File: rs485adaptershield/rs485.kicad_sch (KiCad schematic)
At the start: 13 parts, among them U10 MAX485E

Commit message: more work
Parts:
- removed C1: 100n, Capacitor_SMD:C_0805_2012Metric, symbol Device:C
- removed R2, R3, R4: 10k, Resistor_SMD:R_0805_2012Metric, symbol Device:R
- removed U10: MAX485E, Package_SO:SOIC-8_3.9x4.9mm_P1.27mm, symbol Interface_UART:MAX485E
- added C21: 100n, Capacitor_SMD:C_0603_1608Metric, symbol Device:C
- added IC2: THVD1406DRLR, SOTFL50P160X60-8N, symbol THVD1406DRLR:THVD1406DRLR
- added R13: 10k, Resistor_SMD:R_0805_2012Metric, symbol Device:R
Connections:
- net DI is gone; now on net ¬RE: R5.2
- net +5V: now also C21.2, IC2.8 (VCC), R13.1
- net GND: now also C21.1, IC2.5 (GND)
- net ¬RE: now also IC2.2 (~{RE})
- net A+ renamed A
- net B- renamed B
- new net: IC2.3 (~{SHDN}), R13.2
- new net D: IC2.4 (D)
- new net R: IC2.1 (R)
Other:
- moved on the sheet: D2, D3, F2, F3, R6, R7, R8

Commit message: more progress
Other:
- moved on the sheet: C21, D2, D3, F2, F3, IC2, R13, R5, R6, R7, R8

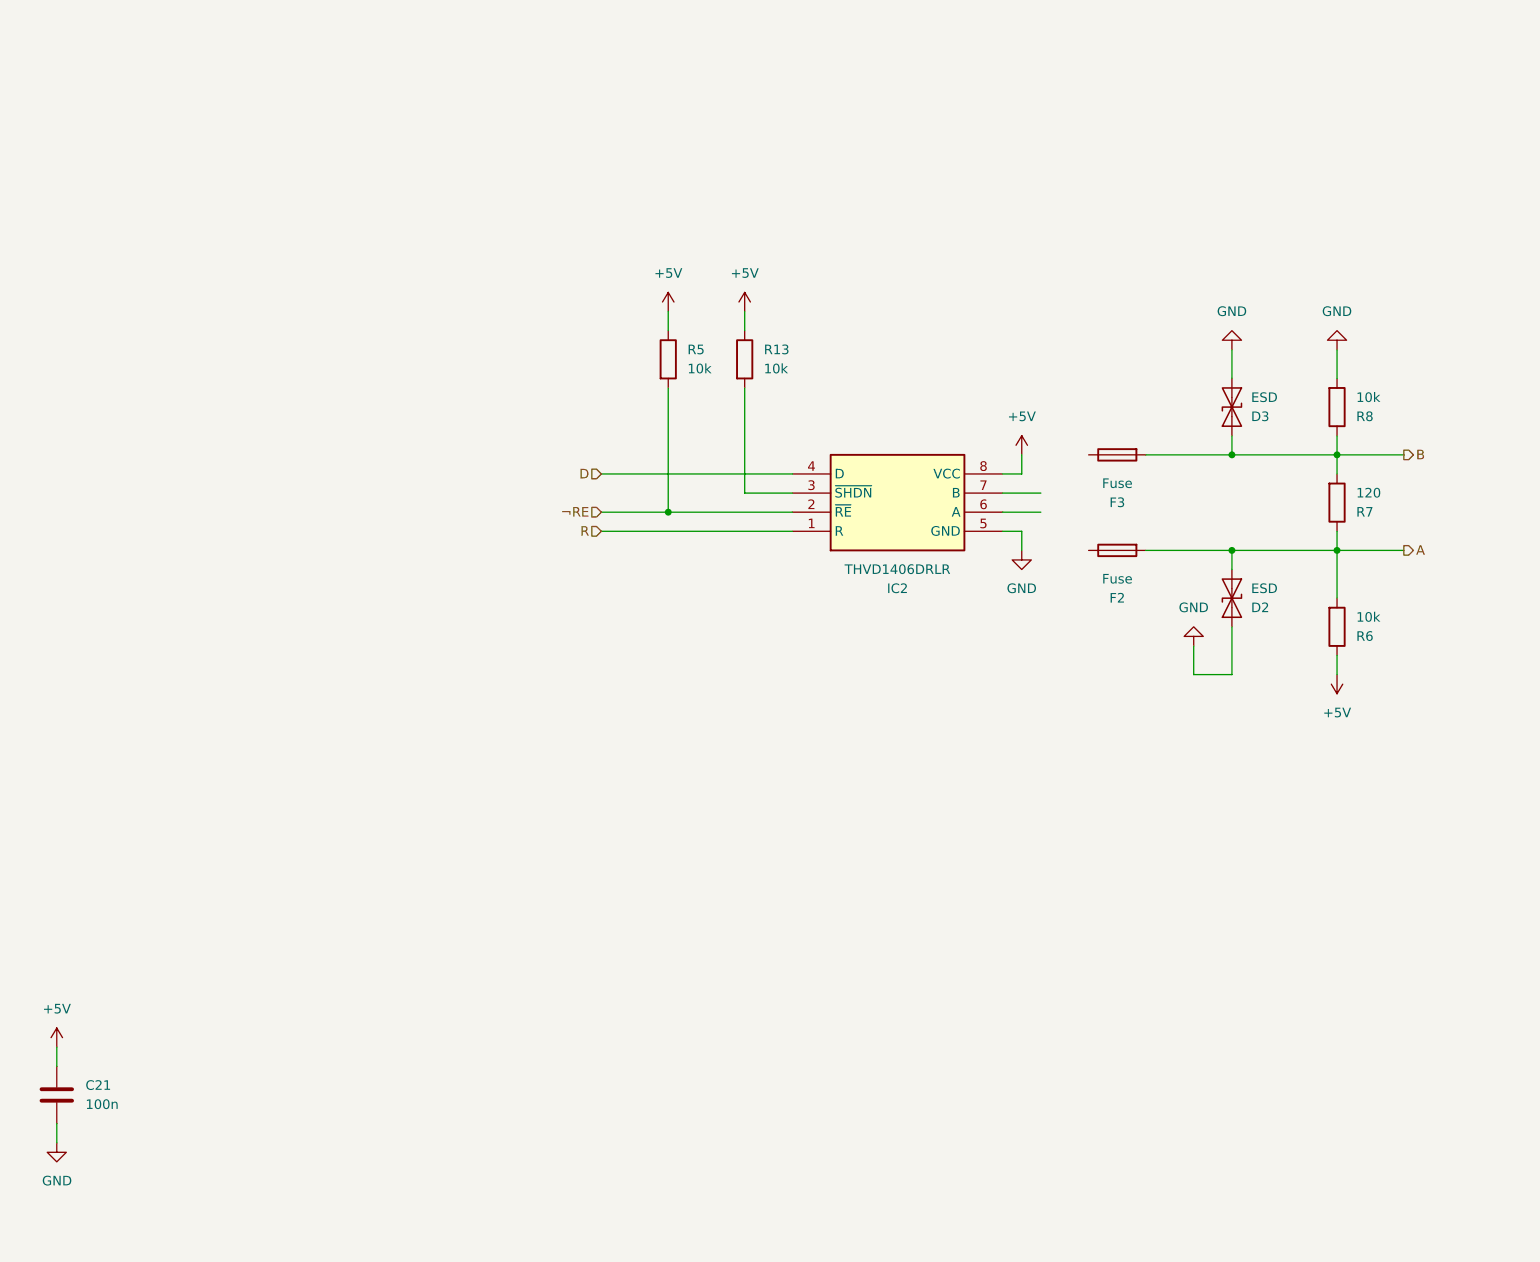
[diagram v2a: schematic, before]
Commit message: schematic mostly finished w/o footprints
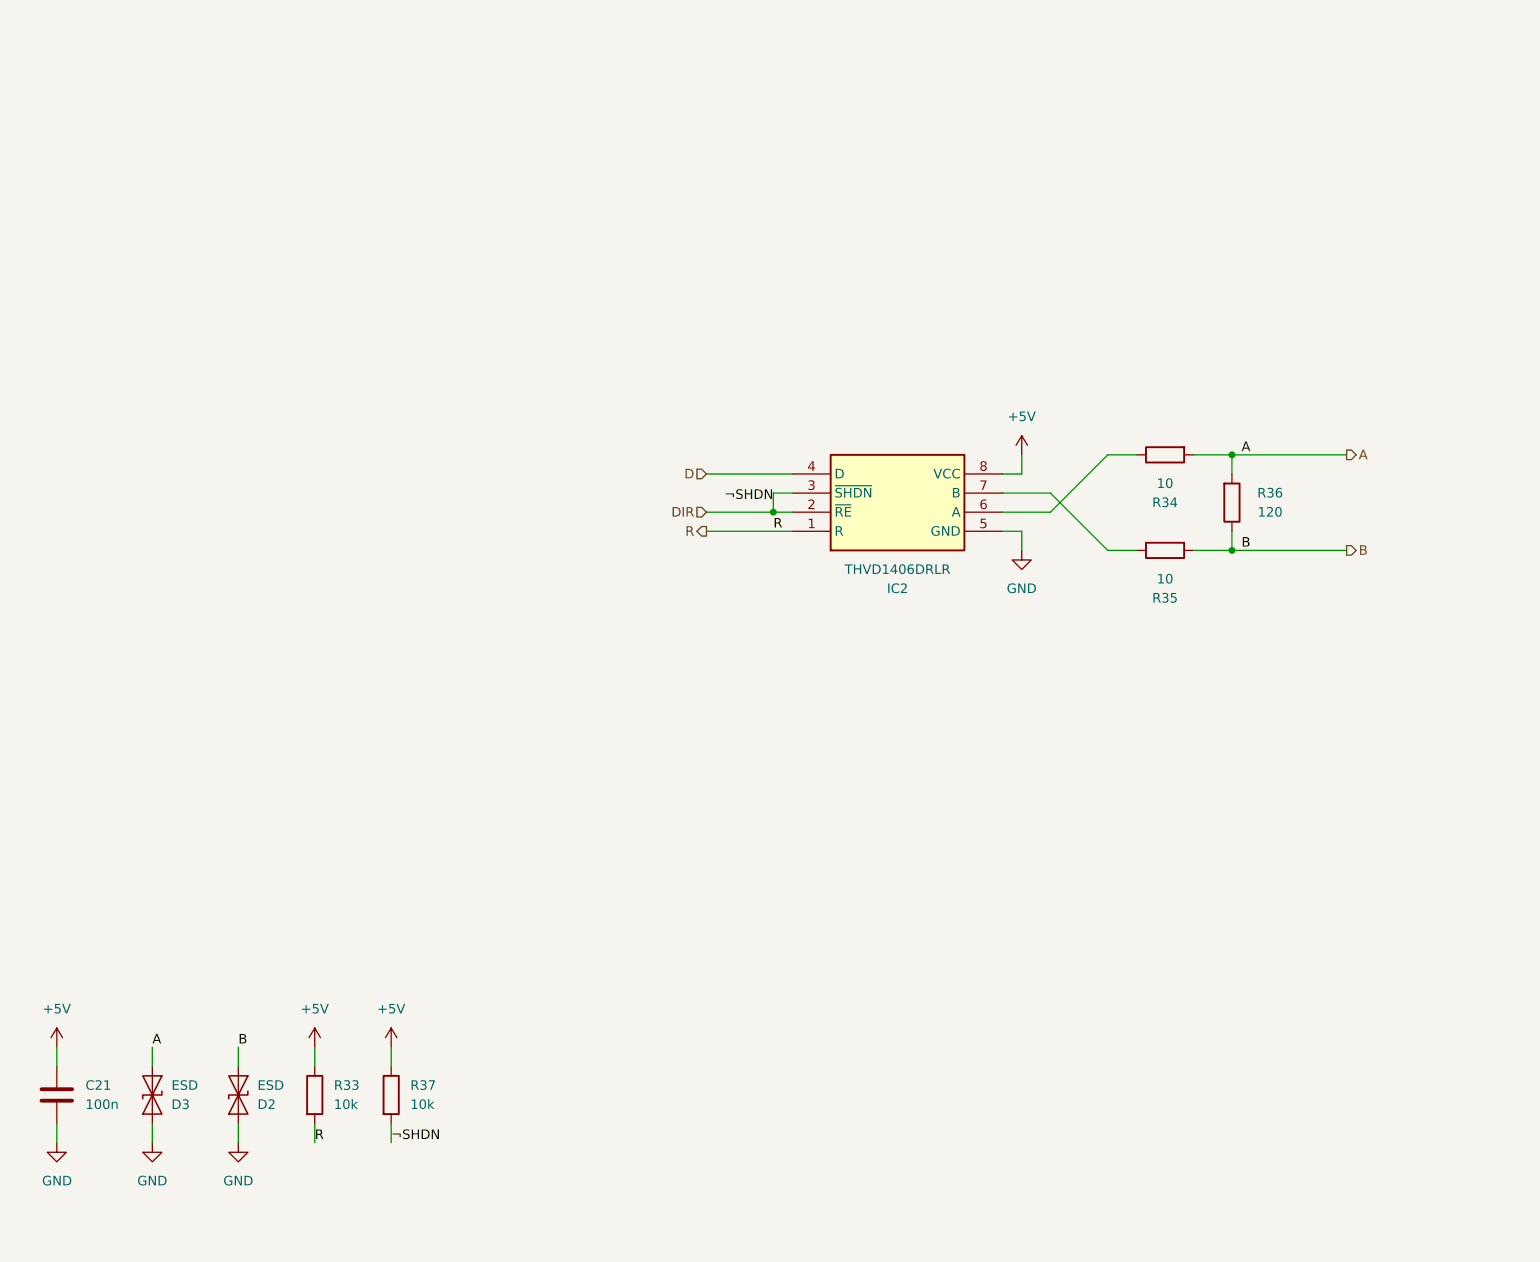
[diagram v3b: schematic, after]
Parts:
- removed F2, F3: Fuse, Fuse:Fuse_1812_4532Metric, symbol Device:Fuse
- removed R13, R5, R6, R8: 10k, Resistor_SMD:R_0805_2012Metric, symbol Device:R
- removed R7: 120, Resistor_SMD:R_0805_2012Metric, symbol Device:R
- added R33, R37: 10k, Capacitor_SMD:C_0402_1005Metric, symbol Device:R
- added R34, R35: 10, Capacitor_SMD:C_0402_1005Metric, symbol Device:R
- added R36: 120, Capacitor_SMD:C_0402_1005Metric, symbol Device:R
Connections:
- net ¬RE is gone; now on net DIR: IC2.2 (~{RE})
- net +5V: now also R33.1, R37.1
- net A: now also D3.1 (A1), R34.2, R36.2; no longer D2.2 (A2)
- net B: now also D2.2 (A2), R35.2, R36.1; no longer D3.2 (A2)
- net GND: now also D3.2 (A2); no longer D3.1 (A1)
- net R: now also R33.2
- net DIR: now reaches IC2.3 (~{SHDN})
- net DIR: now also R37.2
- net at IC2.6 (A): now also R34.1
- net at IC2.7 (B): now also R35.1

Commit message: usb stackup problems
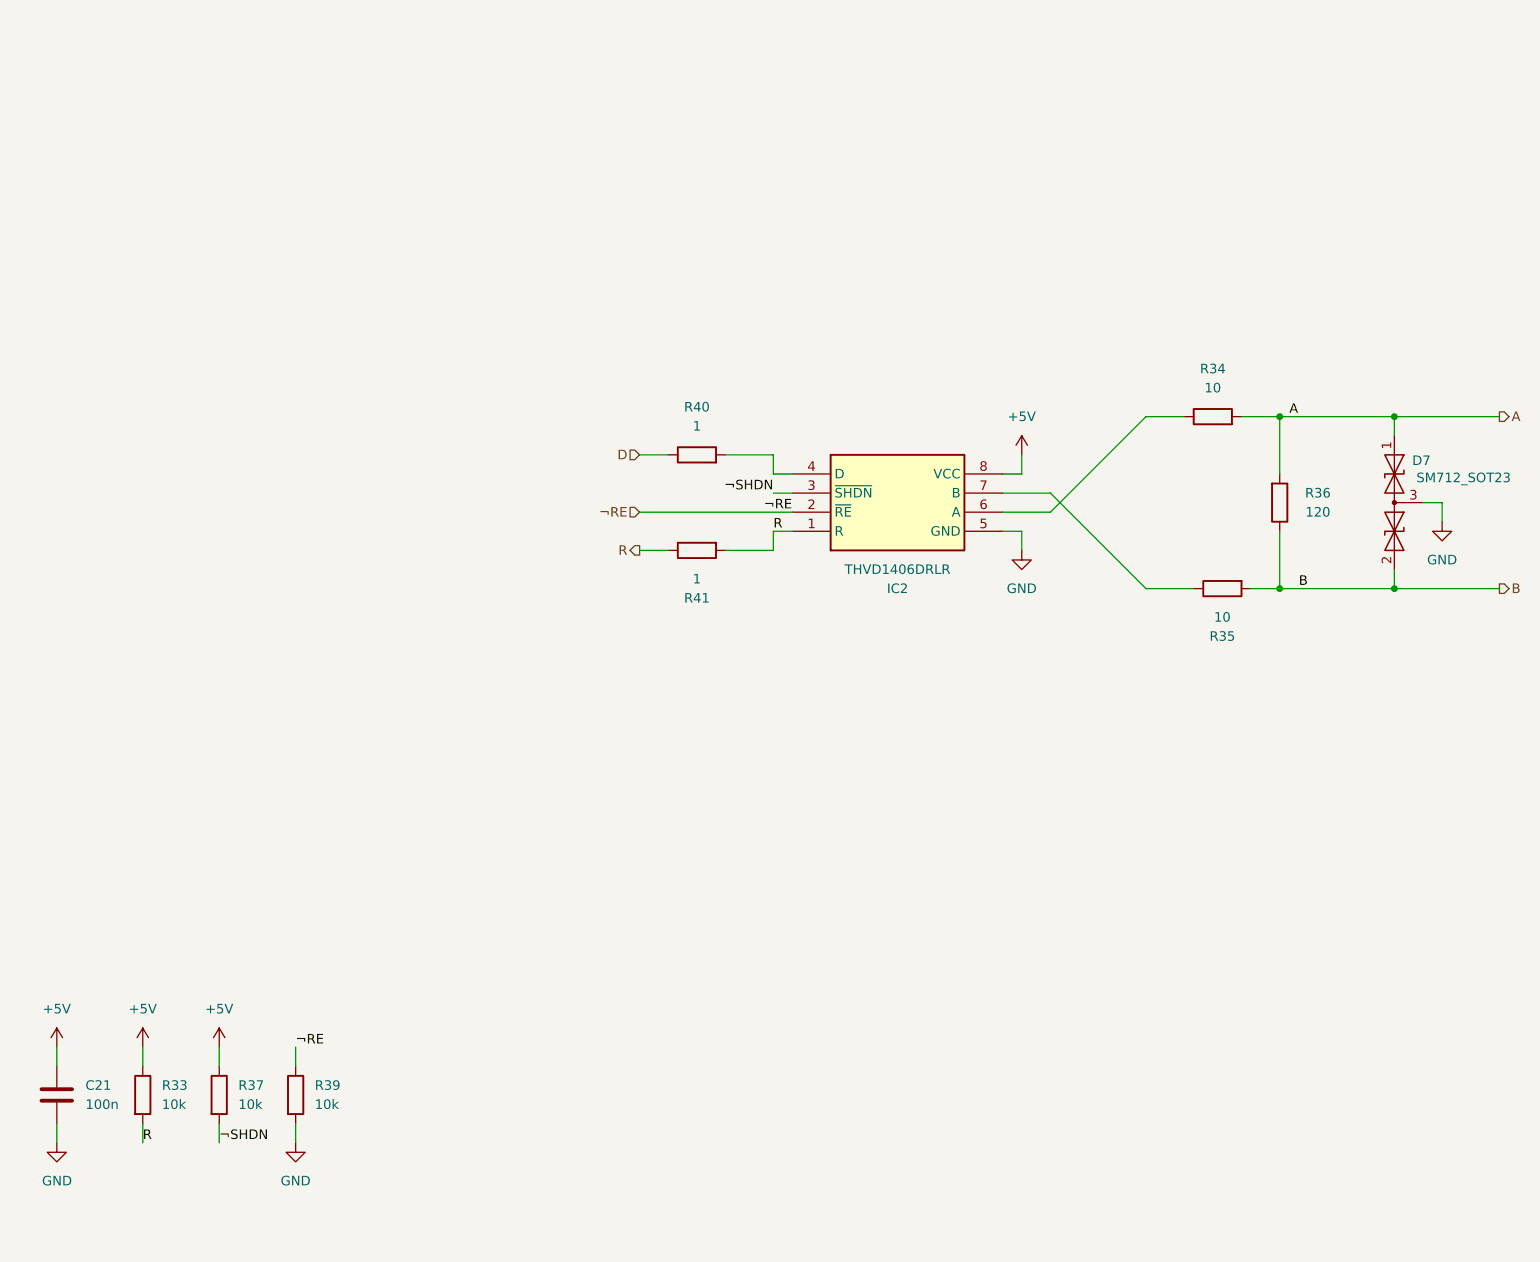
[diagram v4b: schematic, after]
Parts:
- removed D2, D3: ESD, Diode_SMD:D_SMA, symbol Diode:ESD131-B1-W0201
- added D7: SM712_SOT23, Package_TO_SOT_SMD:SOT-23, symbol Diode:SM712_SOT23
- added R39: 10k, Resistor_SMD:R_0402_1005Metric, symbol Device:R
- added R40, R41: 1, Resistor_SMD:R_0603_1608Metric, symbol Device:R
- C21: footprint Capacitor_SMD:C_0603_1608Metric -> Capacitor_SMD:C_0402_1005Metric
- IC2: footprint SOTFL50P160X60-8N -> Package_TO_SOT_SMD:SOT-23-8
- R33, R37: footprint Capacitor_SMD:C_0402_1005Metric -> Resistor_SMD:R_0402_1005Metric
- R34, R35: footprint Capacitor_SMD:C_0402_1005Metric -> Resistor_SMD:R_0603_1608Metric
- R36: footprint Capacitor_SMD:C_0402_1005Metric -> Resistor_SMD:R_0805_2012Metric
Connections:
- net A: now also D7.1 (A1)
- net B: now also D7.2 (A2)
- net D: now also R40.1; no longer IC2.4 (D)
- net GND: now also D7.3 (common), R39.2
- net R: now also R41.1, R41.2
- net DIR renamed ¬SHDN
- net ¬SHDN: no longer IC2.2 (~{RE})
- new net: IC2.4 (D), R40.2
- new net ¬RE: IC2.2 (~{RE}), R39.1
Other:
- moved on the sheet: R33, R34, R35, R36, R37

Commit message: pushes
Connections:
- net R: no longer IC2.1 (R), R33.2, R41.2
- net TX: now reaches IC2.4 (D), R40.2
- net ¬SHDN renamed ¬SHUTDOWN
- new net RX: IC2.1 (R), R33.2, R41.2
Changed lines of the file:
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@@
 		)
 	)
-	(label "B"
-		(at 194.31 109.22 0)
+	(label "TX"
+		(at 124.46 93.98 0)
 		(effects
 			(font
@@
 		)
 	)
-	(label "R"
-		(at 40.64 182.88 0)
+	(label "B"
+		(at 193.04 109.22 0)
 		(effects
 			(font
@@
 		)
 	)
-	(label "¬RE"
-		(at 123.19 99.06 0)
+	(label "¬RESET"
+		(at 60.96 170.18 90)
 		(effects
 			(font
@@
 		)
 	)
-	(label "¬RE"
-		(at 60.96 170.18 0)
+	(label "¬RESET"
+		(at 116.84 99.06 0)
+		(effects
+			(font
+				(size 1.27 1.27)
+			)
+			(justify left bottom)
+		)
+	)
+	(label "¬SHUTDOWN"
+		(at 50.8 182.88 270)
+		(effects
+			(font
+				(size 1.27 1.27)
+			)
+			(justify right bottom)
+		)
+	)
+	(label "RX"
+		(at 124.46 104.14 0)
 		(effects
 			(font
@@
 		)
 	)
-	(label "¬SHDN"
+	(label "¬SHUTDOWN"
 		(at 124.46 96.52 180)
 		(effects
@@
 		)
 	)
-	(label "R"
-		(at 124.46 101.6 0)
+	(label "RX"
+		(at 40.64 182.88 270)
 		(effects
 			(font
 				(size 1.27 1.27)
 			)
-			(justify left bottom)
+			(justify right bottom)
 		)
 	)
-	(label "¬SHDN"
-		(at 50.8 182.88 0)
-		(effects
-			(font
-				(size 1.27 1.27)
-			)
-			(justify left bottom)
-		)
-	)

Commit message: more layout
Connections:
- net +5V renamed +3.3V
